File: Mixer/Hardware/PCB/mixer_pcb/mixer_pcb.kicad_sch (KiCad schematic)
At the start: 37 parts, among them J1 THONKICONN, J2 THONKICONN, J3 THONKICONN, J4 THONKICONN, J5 THONKICONN, J6 THONKICONN, J7 Eurorack_2x5_Power, J8 Conn_01x02_Socket, J9 Conn_01x02_Socket, SW1 TAIWAY 200CWMSP1T3B4M2, SW2 TAIWAY 200CWMSP1T3B4M2, SW3 TAIWAY 200CWMSP1T3B4M2, SW4 TAIWAY 200CWMSP1T3B4M2, SW5 TAIWAY 200CWMSP1T3B4M2, U1 Opamp_Dual

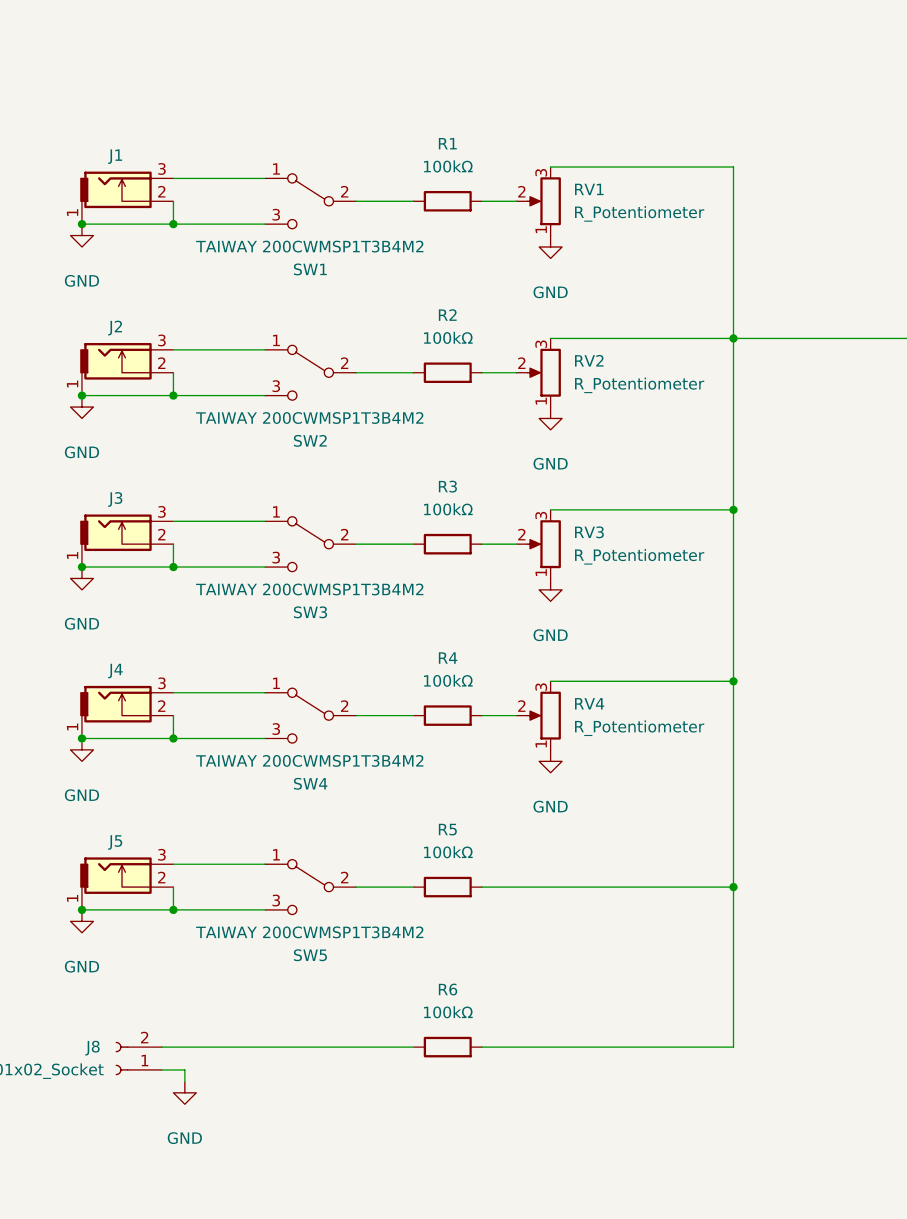
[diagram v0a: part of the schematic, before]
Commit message: Fix some bugs in the new Mixer PCB
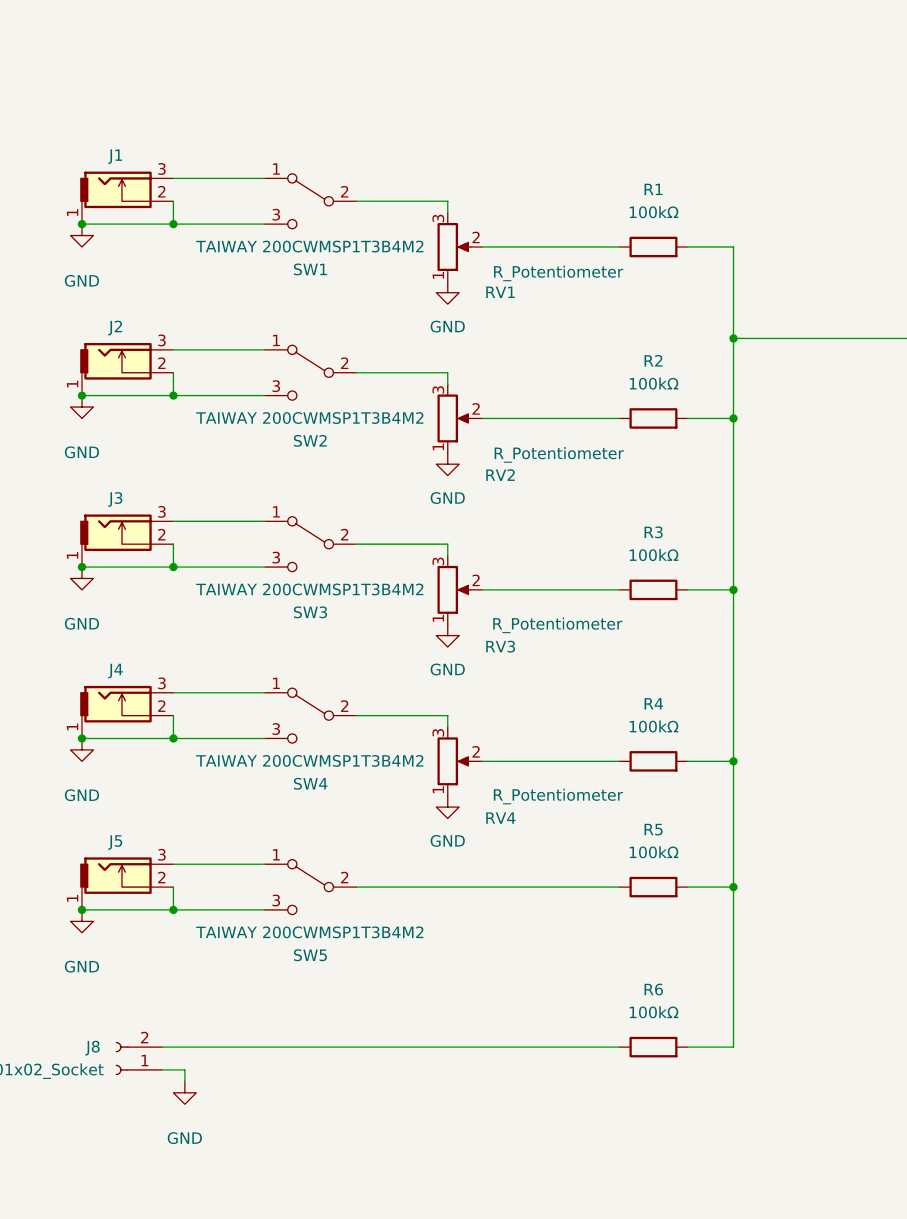
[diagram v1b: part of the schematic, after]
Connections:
- net at R3.1: now also RV3.2; no longer SW3.2 (B)
- net at R3.2: now also C3.1, R1.2, R2.2, R4.2, R5.2, R6.2, R7.1, U1.3 (+); no longer RV3.2
- net at SW4.2 (B): now also RV4.3; no longer R4.1
- net at RV4.2: now also R4.1; no longer R4.2
- net at SW2.2 (B): now also RV2.3; no longer R2.1
- net at RV2.2: now also R2.1; no longer R2.2
- net at SW1.2 (B): now also RV1.3; no longer R1.1
- net at RV1.2: now also R1.1; no longer R1.2
- new net: RV3.3, SW3.2 (B)
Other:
- moved on the sheet: R1, R2, R3, R4, R5, R6, RV1, RV2, RV3, RV4
